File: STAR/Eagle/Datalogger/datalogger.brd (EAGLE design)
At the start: 26.4 x 55.9 mm, 7 parts, among them J1 J30J-25

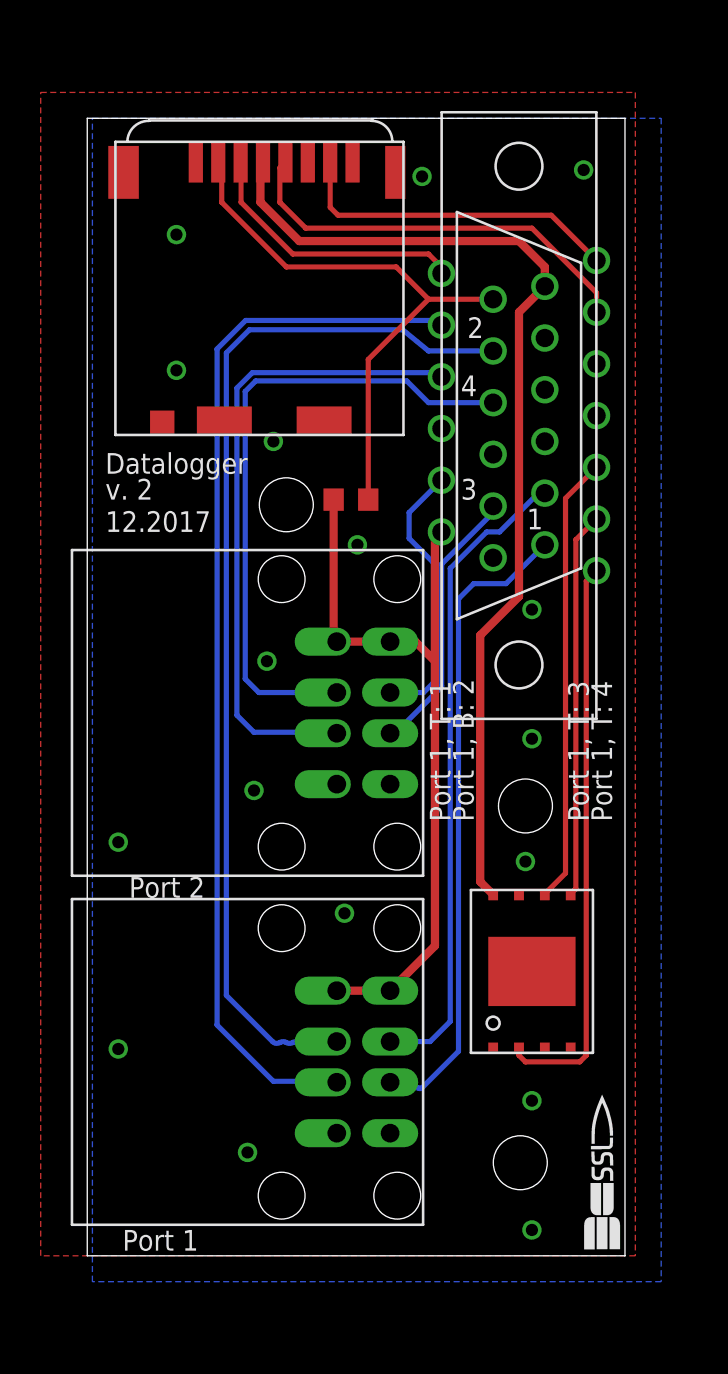
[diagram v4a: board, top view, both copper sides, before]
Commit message: M2 drills
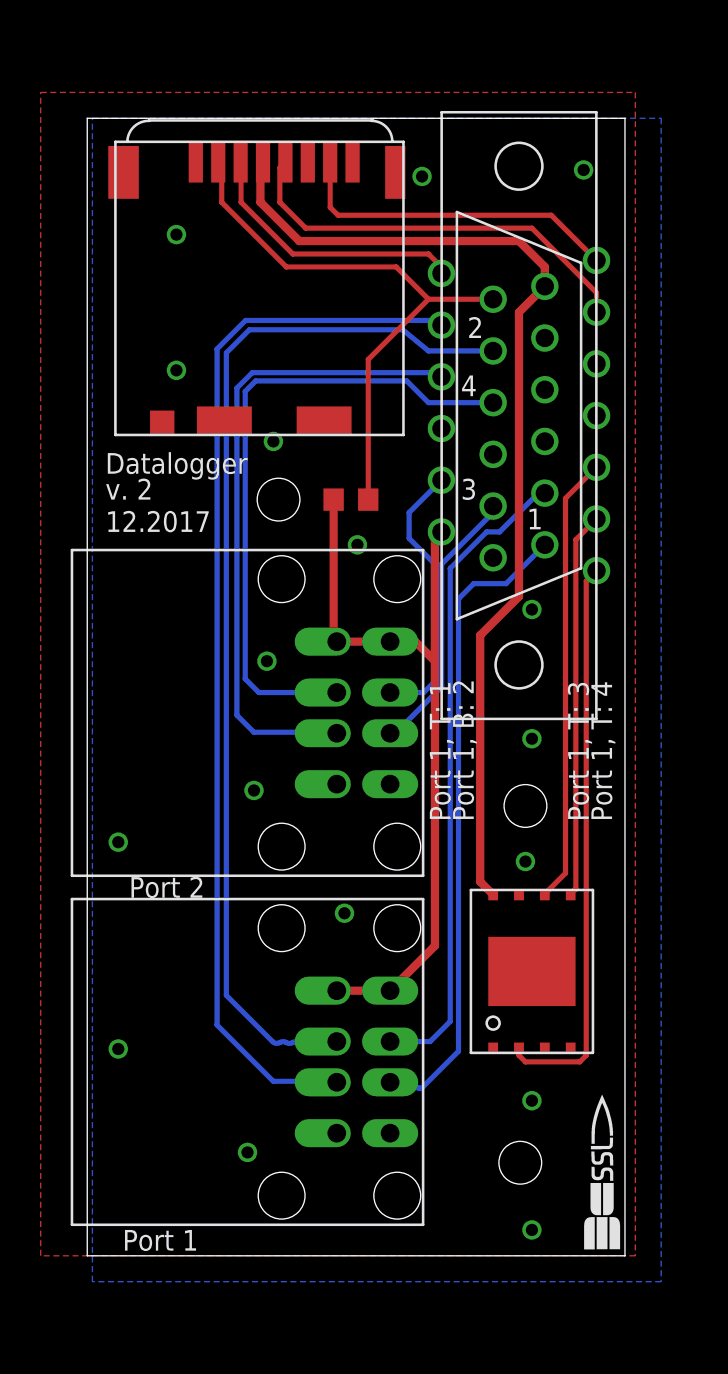
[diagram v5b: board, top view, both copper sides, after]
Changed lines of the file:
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@@
 <text x="11.684" y="6.096" size="1.016" layer="21" font="vector" rot="R90">Port 1, T: 3</text>
 <text x="12.827" y="6.096" size="1.016" layer="21" font="vector" rot="R90">Port 1, T: 4</text>
-<hole x="8.5725" y="6.858" drill="2.65"/>
-<hole x="8.3185" y="-10.668" drill="2.65"/>
-<hole x="-3.175" y="21.6535" drill="2.65"/>
+<hole x="8.5725" y="6.858" drill="2.1"/>
+<hole x="8.3185" y="-10.668" drill="2.1"/>
+<hole x="-3.556" y="21.9075" drill="2.1"/>
 </plain>
 <attributes>

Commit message: got rid of old STARduino routing
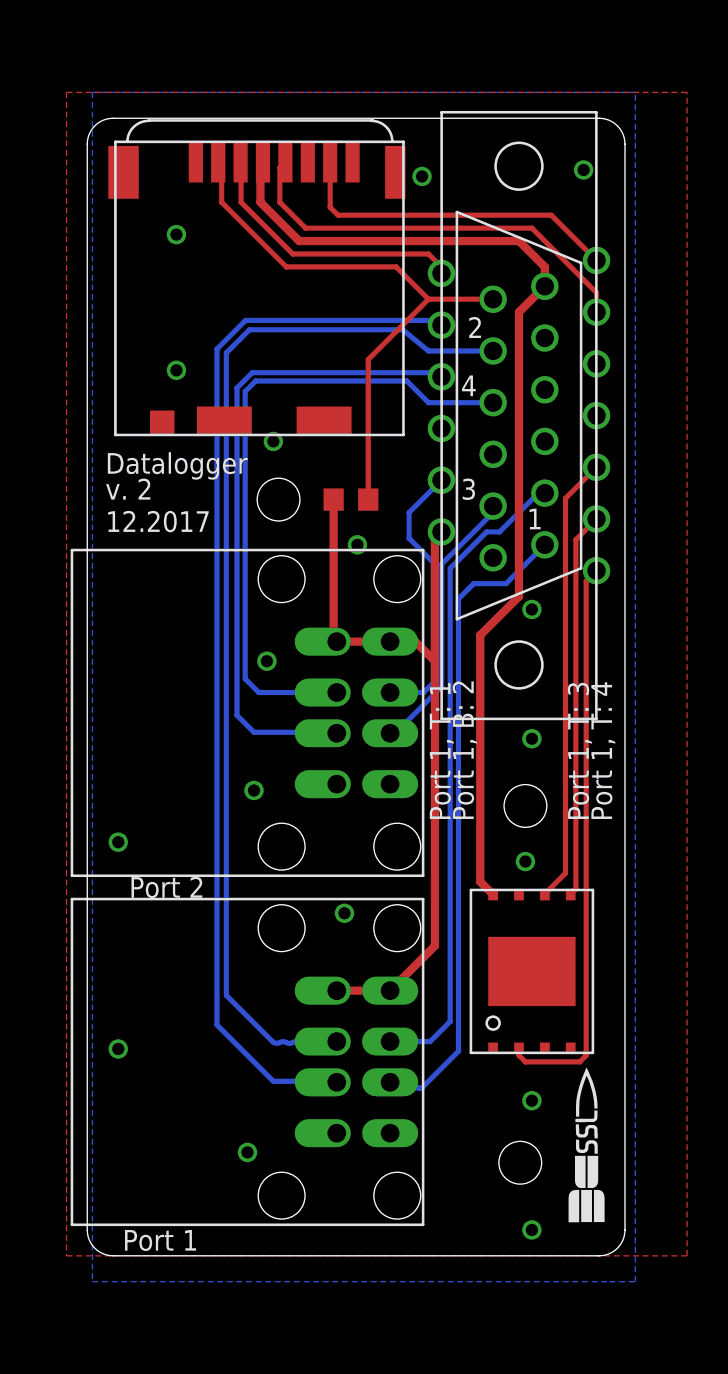
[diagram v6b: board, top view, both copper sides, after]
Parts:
- moved U$4 1.54 mm to (10.4, -13.6)
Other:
- outline, holes or cut-outs redrawn
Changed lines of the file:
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@@
 <board>
 <plain>
-<wire x1="-12.954" y1="-15.24" x2="13.462" y2="-15.24" width="0" layer="20"/>
-<wire x1="13.462" y1="-15.24" x2="13.462" y2="40.64" width="0" layer="20"/>
-<wire x1="13.462" y1="40.64" x2="-12.954" y2="40.64" width="0" layer="20"/>
-<wire x1="-12.954" y1="40.64" x2="-12.954" y2="-15.24" width="0" layer="20"/>
+<wire x1="-11.684" y1="-15.24" x2="12.192" y2="-15.24" width="0" layer="20"/>
+<wire x1="13.462" y1="-13.97" x2="13.462" y2="39.37" width="0" layer="20"/>
+<wire x1="12.192" y1="40.64" x2="-11.684" y2="40.64" width="0" layer="20"/>
 <text x="-12.065" y="23.1775" size="1.016" layer="21" font="vector">Datalogger</text>
 <text x="-12.065" y="21.9075" size="1.016" layer="21" font="vector">v. 2</text>
@@
 <hole x="8.3185" y="-10.668" drill="2.1"/>
 <hole x="-3.556" y="21.9075" drill="2.1"/>
+<wire x1="-12.954" y1="39.37" x2="-12.954" y2="-13.97" width="0" layer="20"/>
+<wire x1="-11.684" y1="-15.24" x2="-12.954" y2="-13.97" width="0" layer="20" curve="-90"/>
+<wire x1="13.462" y1="-13.97" x2="12.192" y2="-15.24" width="0" layer="20" curve="-90"/>
+<wire x1="12.192" y1="40.64" x2="13.462" y2="39.37" width="0" layer="20" curve="-90"/>
+<wire x1="-11.684" y1="40.64" x2="-12.954" y2="39.37" width="0" layer="20" curve="90"/>
 </plain>
 <attributes>
@@
 <element name="U$2" library="NR_connectors" package="USB_A" value="USB_A" x="-5.08" y="-5.715" smashed="yes" rot="R270"/>
 <element name="U$3" library="NR_connectors" package="USB_A" value="USB_A" x="-5.08" y="11.43" smashed="yes" rot="R270"/>
-<element name="U$4" library="images" package="SSL_SILK_.3IN" value="SSL.3IN_SILK" x="11.1125" y="-14.9225"/>
+<element name="U$4" library="images" package="SSL_SILK_.3IN" value="SSL.3IN_SILK" x="10.3505" y="-13.589"/>
 <element name="U$5" library="NR_IC" package="WSON" value="W25N01GV" x="8.89" y="-1.27" smashed="yes" rot="R90"/>
 </elements>
@@
 <via x="3.4925" y="37.7825" extent="1-16" drill="0.6"/>
 <polygon width="0.4064" layer="16">
-<vertex x="-12.7" y="40.64"/>
-<vertex x="15.24" y="40.64"/>
-<vertex x="15.24" y="-16.51"/>
+<vertex x="-12.7" y="41.91"/>
 <vertex x="-12.7" y="-16.51"/>
+<vertex x="12.7" y="-16.51"/>
+<vertex x="13.97" y="-16.51"/>
+<vertex x="13.97" y="41.91"/>
 </polygon>
 <polygon width="0.4064" layer="1">
-<vertex x="-15.24" y="41.91"/>
-<vertex x="13.97" y="41.91"/>
-<vertex x="13.97" y="-15.24"/>
-<vertex x="-15.24" y="-15.24"/>
+<vertex x="-13.97" y="41.91"/>
+<vertex x="-13.97" y="-15.24"/>
+<vertex x="16.51" y="-15.24"/>
+<vertex x="16.51" y="41.91"/>
 </polygon>
 </signal>

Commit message: misc board stuff
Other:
- board text added: "1.2018"
- board text removed: "12.2017"
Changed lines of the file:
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@@
 <layer number="27" name="tValues" color="7" fill="1" visible="yes" active="yes"/>
 <layer number="28" name="bValues" color="7" fill="1" visible="yes" active="yes"/>
-<layer number="29" name="tStop" color="7" fill="3" visible="no" active="yes"/>
+<layer number="29" name="tStop" color="7" fill="3" visible="yes" active="yes"/>
 <layer number="30" name="bStop" color="7" fill="6" visible="no" active="yes"/>
 <layer number="31" name="tCream" color="7" fill="4" visible="no" active="yes"/>
@@
 <text x="-12.065" y="23.1775" size="1.016" layer="21" font="vector">Datalogger</text>
 <text x="-12.065" y="21.9075" size="1.016" layer="21" font="vector">v. 2</text>
-<text x="-12.065" y="20.32" size="1.016" layer="21" font="vector">12.2017</text>
+<text x="-12.065" y="20.32" size="1.016" layer="21" font="vector">1.2018</text>
 <text x="8.636" y="20.447" size="1.016" layer="21" font="vector">1</text>
 <text x="5.715" y="29.845" size="1.016" layer="21" font="vector">2</text>
@@
 </class>
 </classes>
-<designrules name="OshPark">
+<designrules name="OshPark *">
 <description language="de">&lt;b&gt;EAGLE Design Rules&lt;/b&gt;
 &lt;p&gt;
@@
 <param name="mlMinCreamFrame" value="0mil"/>
 <param name="mlMaxCreamFrame" value="0mil"/>
-<param name="mlViaStopLimit" value="0mil"/>
+<param name="mlViaStopLimit" value="25mil"/>
 <param name="srRoundness" value="0"/>
 <param name="srMinRoundness" value="0mil"/>

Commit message: screws
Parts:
- moved R2 1.53 mm to (1.40, 22.5), turned to 270 degrees
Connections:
- removed net F: J1.9
- removed net J: J1.6
- removed net R: J1.14
- removed net S: J1.7
- removed net V: J1.8
- removed net Y: J1.10
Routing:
- net SD_STAR: track 28.4 -> 26.7 mm
- net +5V: track 38.5 -> 39.0 mm
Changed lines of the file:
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@@
 <hole x="8.5725" y="6.858" drill="2.1"/>
 <hole x="8.3185" y="-10.668" drill="2.1"/>
-<hole x="-3.556" y="21.9075" drill="2.1"/>
+<hole x="-3.429" y="22.0345" drill="2.1"/>
 <wire x1="-12.954" y1="39.37" x2="-12.954" y2="-13.97" width="0" layer="20"/>
 <wire x1="-11.684" y1="-15.24" x2="-12.954" y2="-13.97" width="0" layer="20" curve="-90"/>
@@
 <wire x1="12.192" y1="40.64" x2="13.462" y2="39.37" width="0" layer="20" curve="-90"/>
 <wire x1="-11.684" y1="40.64" x2="-12.954" y2="39.37" width="0" layer="20" curve="90"/>
+<circle x="-3.429" y="22.0345" radius="1.9" width="0.4064" layer="51"/>
+<circle x="8.5725" y="6.858" radius="1.9" width="0.4064" layer="51"/>
+<circle x="8.3185" y="-10.668" radius="1.9" width="0.4064" layer="51"/>
 </plain>
 <attributes>
@@
 <elements>
 <element name="J1" library="CM_J30J" package="ZKN-25" value="J30J-25" x="8.255" y="26.035" smashed="yes" rot="R90"/>
-<element name="R2" library="resistor" package="R0603" value="1M" x="0" y="21.9075" smashed="yes" rot="R180">
-<attribute name="VALUE" x="0.508" y="24.0665" size="1.016" layer="27" font="vector" rot="R180"/>
+<element name="R2" library="resistor" package="R0603" value="1M" x="1.397" y="22.5425" smashed="yes" rot="R270">
+<attribute name="VALUE" x="-0.762" y="23.0505" size="1.016" layer="27" font="vector" rot="R270"/>
 </element>
 <element name="U$1" library="NR_connectors" package="MICRO_SD_HINGED" value="MICRO_SD" x="-7.62" y="25.0825" smashed="yes" rot="R180"/>
@@
 <via x="-0.3175" y="1.5875" extent="1-16" drill="0.6"/>
 <via x="-4.1275" y="13.97" extent="1-16" drill="0.6"/>
-<via x="0.3175" y="19.685" extent="1-16" drill="0.6"/>
+<via x="-1.0795" y="19.4945" extent="1-16" drill="0.6"/>
 <via x="8.89" y="16.51" extent="1-16" drill="0.6"/>
 <via x="11.43" y="38.1" extent="1-16" drill="0.6"/>
@@
 <wire x1="2.2225" y1="33.3375" x2="3.81" y2="31.75" width="0.254" layer="1"/>
 <wire x1="3.81" y1="31.75" x2="6.985" y2="31.75" width="0.254" layer="1"/>
-<wire x1="0.85" y1="21.9075" x2="0.85" y2="28.79" width="0.254" layer="1"/>
-<wire x1="0.85" y1="28.79" x2="3.81" y2="31.75" width="0.254" layer="1"/>
+<wire x1="1.397" y1="23.3925" x2="1.485" y2="29.4885" width="0.254" layer="1"/>
+<wire x1="1.485" y1="29.4885" x2="3.81" y2="31.75" width="0.254" layer="1"/>
 </signal>
 <signal name="MISO_STAR">
@@
 <wire x1="1.925" y1="14.93" x2="-0.695" y2="14.93" width="0.4064" layer="1"/>
 <wire x1="1.925" y1="-2.215" x2="-0.695" y2="-2.215" width="0.4064" layer="1"/>
-<wire x1="-0.85" y1="21.9075" x2="-0.85" y2="15.085" width="0.4064" layer="1"/>
-<wire x1="-0.85" y1="15.085" x2="-0.695" y2="14.93" width="0.4064" layer="1"/>
 <wire x1="1.925" y1="14.93" x2="3.1675" y2="14.93" width="0.4064" layer="1"/>
 <wire x1="3.1675" y1="14.93" x2="4.1275" y2="13.97" width="0.4064" layer="1"/>
@@
 <contactref element="J1" pad="15"/>
 <wire x1="4.1275" y1="20.0025" x2="4.445" y2="20.32" width="0.4064" layer="1"/>
+<wire x1="1.397" y1="21.6925" x2="1.397" y2="20.066" width="0.4064" layer="1"/>
+<wire x1="1.397" y1="20.066" x2="0" y2="18.669" width="0.4064" layer="1"/>
+<wire x1="0" y1="18.669" x2="0" y2="15.625" width="0.4064" layer="1"/>
+<wire x1="0" y1="15.625" x2="-0.695" y2="14.93" width="0.4064" layer="1"/>
 </signal>
 <signal name="DATA1_P">
@@
 <wire x1="11.557" y1="17.907" x2="12.065" y2="18.415" width="0.254" layer="1"/>
 </signal>
-<signal name="F">
-<contactref element="J1" pad="9"/>
-</signal>
-<signal name="Y">
-<contactref element="J1" pad="10"/>
-</signal>
-<signal name="S">
-<contactref element="J1" pad="7"/>
-</signal>
 <signal name="B">
 <contactref element="J1" pad="18"/>
 </signal>
-<signal name="V">
-<contactref element="J1" pad="8"/>
-</signal>
-<signal name="J">
-<contactref element="J1" pad="6"/>
-</signal>
 <signal name="H">
 <contactref element="J1" pad="19"/>
 </signal>
-<signal name="R">
-<contactref element="J1" pad="14"/>
-</signal>
 <signal name="N$10">
